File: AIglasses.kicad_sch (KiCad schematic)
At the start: 7 parts, among them SW2 SW_Push, U4 XIAO-ESP32-C6-SMD, U5 MAX98357A

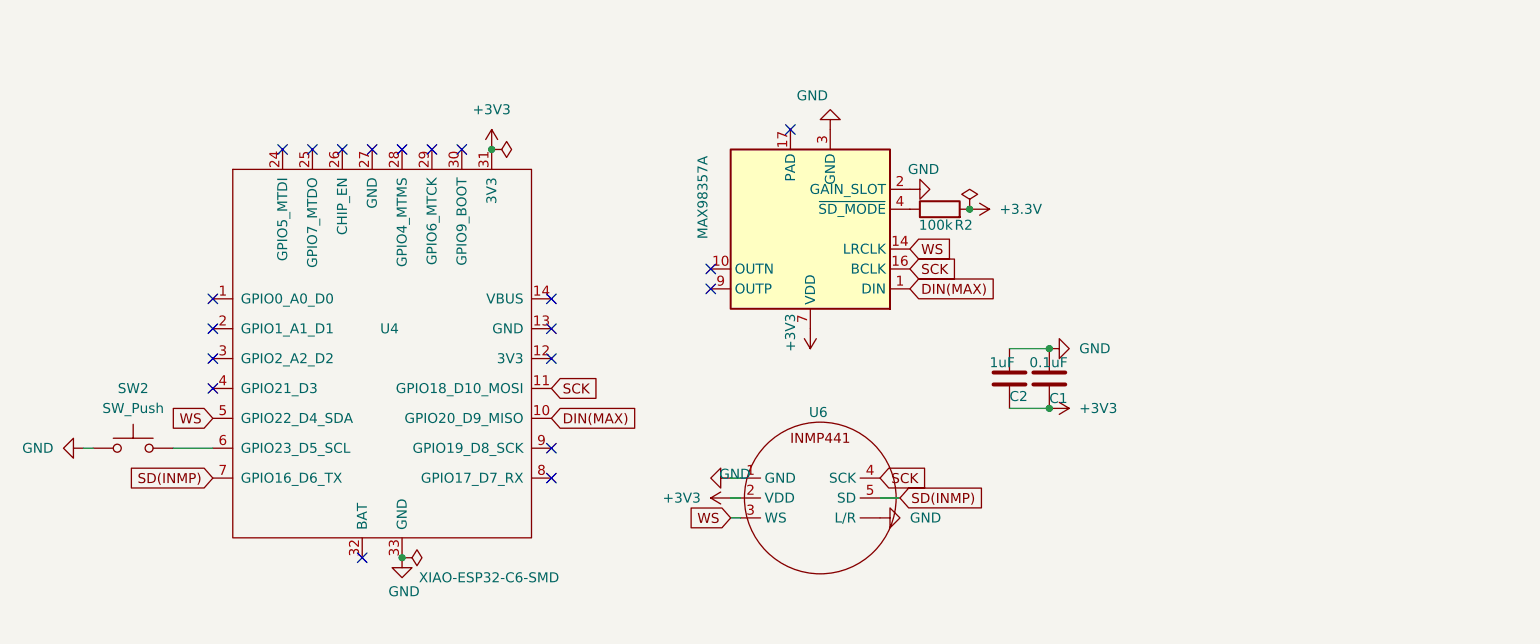
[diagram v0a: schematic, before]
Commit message: Migrated firmware to PlatformIO
Replaced modular architecture with direct .ino-to-src/main.cpp approach.
Both projects build cleanly using the pioarduino ESP32-C6 platform.

Co-Authored-By: Claude Sonnet 4.5 <noreply@anthropic.com>
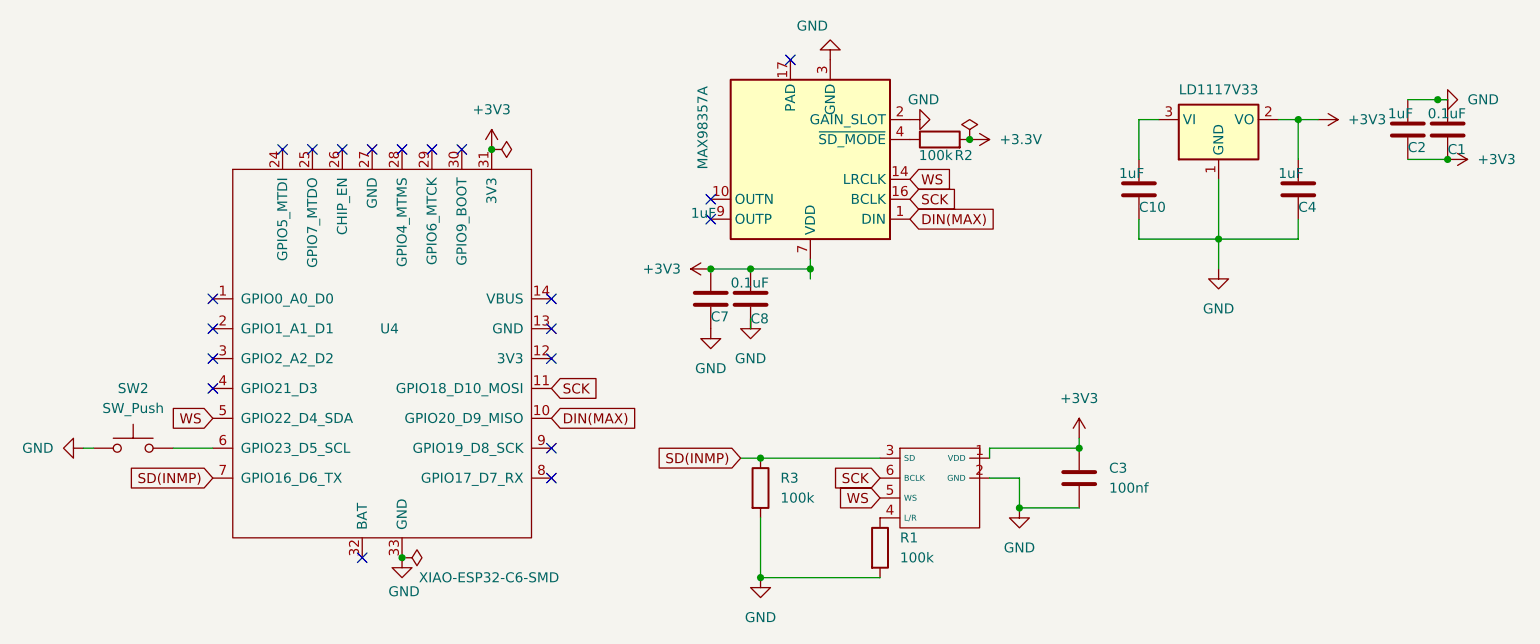
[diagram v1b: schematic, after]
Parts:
- removed U6: ~, symbol Device:INMP441
- added C10, C4, C7: 1uF, symbol Device:C
- added C3: 100nf, symbol Device:C
- added C8: 0.1uF, symbol Device:C
- added R1, R3: 100k, symbol Device:R
- added U2: ~, symbol INMP441:INMP441
- added U3: LD1117V33, Package_TO_SOT_THT:TO-220-3_Vertical, symbol Regulator_Linear:LD1117V33
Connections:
- net +3V3: now also C3.1, C4.1, C7.1, C8.1, U2.1 (VDD), U3.2 (VO)
- net GND: now also C10.2, C3.2, C4.2, C7.2, C8.2, R1.2, R3.2, U2.2 (GND), U3.1 (GND)
- net SCK: now also U2.6 (BCLK)
- net SD(INMP): now also R3.1, U2.3 (SD)
- net WS: now also U2.5 (WS)
- new net: C10.1, U3.3 (VI)
- new net: R1.1, U2.4 (L/R)
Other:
- moved on the sheet: C1, C2, R2
